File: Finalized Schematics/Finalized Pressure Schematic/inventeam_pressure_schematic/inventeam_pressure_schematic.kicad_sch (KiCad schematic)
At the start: 5 parts, among them J1 Conn_02x20_Top_Bottom

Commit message: Pressure V2.1
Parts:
- added TP1, TP10, TP11, TP12, TP13, TP14, TP15, TP16, TP17, TP18, TP19, TP2, TP20, TP21, TP22, TP23, TP24, TP25, TP26, TP27, TP28, TP29, TP3, TP30, TP31, TP32, TP33, TP34, TP35, TP36, TP37, TP38, TP4, TP5, TP6, TP7, TP8, TP9: TestPoint_Probe, TestPoint:TestPoint_Pad_D2.5mm, symbol Connector:TestPoint_Probe
- H1, H2, H3, H4: footprint (none) -> MountingHole:MountingHole_2.7mm_M2.5
- J1: footprint (none) -> Connector_PinHeader_2.54mm:PinHeader_2x20_P2.54mm_Vertical
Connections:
- net COL_1: now also TP1.1
- net COL_10: now also TP10.1
- net COL_11: now also TP11.1
- net COL_12: now also TP12.1
- net COL_13: now also TP13.1
- net COL_14: now also TP14.1
- net COL_15: now also TP15.1
- net COL_16: now also TP16.1
- net COL_17: now also TP17.1
- net COL_18: now also TP18.1
- net COL_19: now also TP19.1
- net COL_2: now also TP2.1
- net COL_20: now also TP20.1
- net COL_21: now also TP21.1
- net COL_22: now also TP22.1
- net COL_23: now also TP23.1
- net COL_24: now also TP24.1
- net COL_25: now also TP25.1
- net COL_26: now also TP26.1
- net COL_3: now also TP3.1
- net COL_4: now also TP4.1
- net COL_5: now also TP5.1
- net COL_6: now also TP6.1
- net COL_7: now also TP7.1
- net COL_8: now also TP8.1
- net COL_9: now also TP9.1
- net ROW_1: now also TP27.1
- net ROW_10: now also TP36.1
- net ROW_11: now also TP37.1
- net ROW_12: now also TP38.1
- net ROW_2: now also TP28.1
- net ROW_3: now also TP29.1
- net ROW_4: now also TP30.1
- net ROW_5: now also TP31.1
- net ROW_6: now also TP32.1
- net ROW_7: now also TP33.1
- net ROW_8: now also TP34.1
- net ROW_9: now also TP35.1
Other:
- sheet Row Matrix renamed Pressure Matrix
- removed sheet Column Matrix
- sheet Pressure Matrix: file row_matrix.kicad_sch -> pressure_matrix.kicad_sch
- sheet Pressure Matrix ports: added COL_1, COL_10, COL_11, COL_12, COL_13, COL_14, COL_15, COL_16, COL_17, COL_18, COL_19, COL_2, COL_20, COL_21, COL_22, COL_23, COL_24, COL_25, COL_26, COL_3, COL_4, COL_5, COL_6, COL_7, COL_8, COL_9; removed none
- note added: "Pressure Matrix"
- note added: "Test Points"
- note removed: "Column Matrix (hierarchical)"
- note removed: "Row Matrix (hierarchical)"
- moved on the sheet: H1, H2, H3, H4

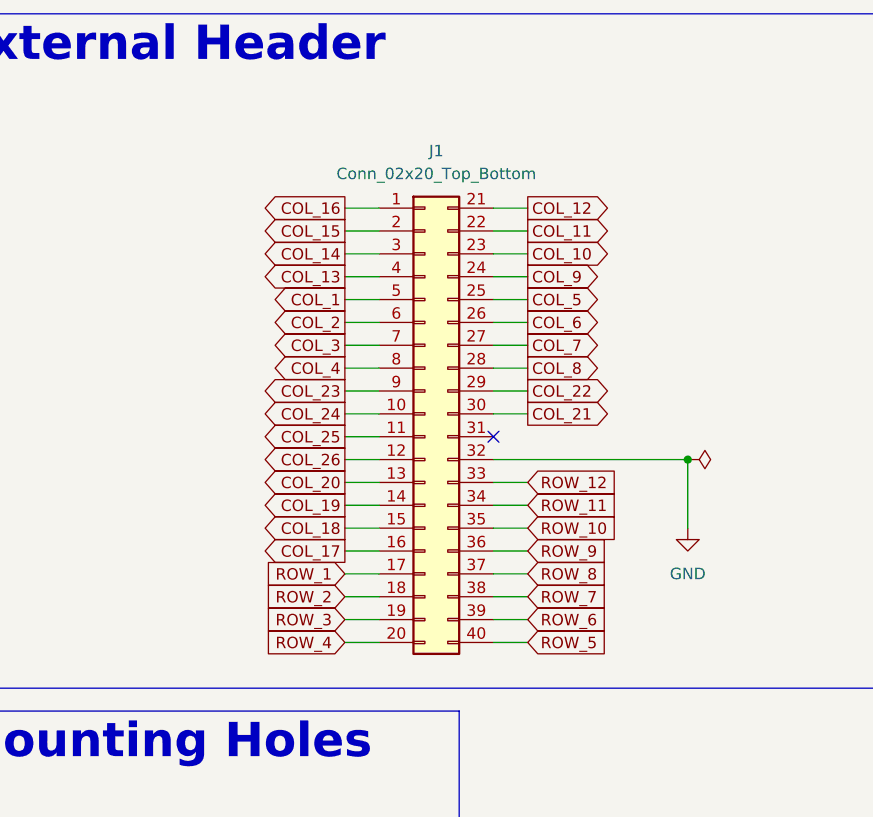
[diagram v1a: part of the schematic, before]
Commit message: Fixed header
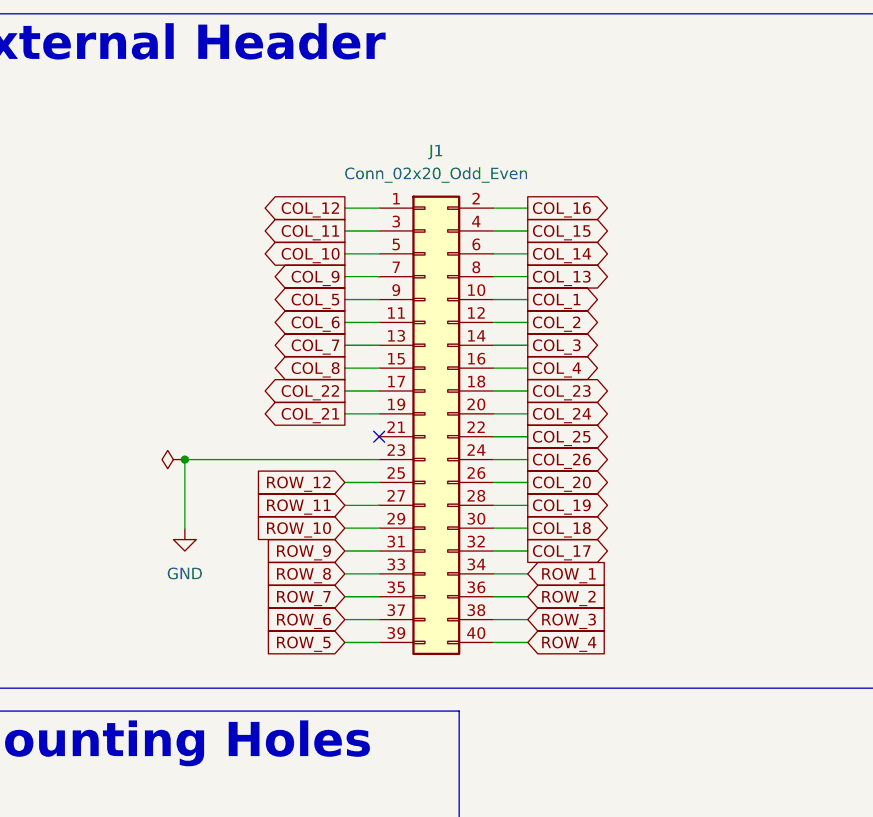
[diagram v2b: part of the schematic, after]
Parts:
- removed J1: Conn_02x20_Top_Bottom, Connector_PinHeader_2.54mm:PinHeader_2x20_P2.54mm_Vertical, symbol Connector_Generic:Conn_02x20_Top_Bottom
- added J1: Conn_02x20_Odd_Even, Connector_PinHeader_2.54mm:PinHeader_2x20_P2.54mm_Vertical, symbol Connector_Generic:Conn_02x20_Odd_Even
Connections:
- net COL_1: now also J1.10 (Pin_10)
- net COL_10: now also J1.5 (Pin_5)
- net COL_11: now also J1.3 (Pin_3)
- net COL_12: now also J1.1 (Pin_1)
- net COL_13: now also J1.8 (Pin_8)
- net COL_14: now also J1.6 (Pin_6)
- net COL_15: now also J1.4 (Pin_4)
- net COL_16: now also J1.2 (Pin_2)
- net COL_17: now also J1.32 (Pin_32)
- net COL_18: now also J1.30 (Pin_30)
- net COL_19: now also J1.28 (Pin_28)
- net COL_2: now also J1.12 (Pin_12)
- net COL_20: now also J1.26 (Pin_26)
- net COL_21: now also J1.19 (Pin_19)
- net COL_22: now also J1.17 (Pin_17)
- net COL_23: now also J1.18 (Pin_18)
- net COL_24: now also J1.20 (Pin_20)
- net COL_25: now also J1.22 (Pin_22)
- net COL_26: now also J1.24 (Pin_24)
- net COL_3: now also J1.14 (Pin_14)
- net COL_4: now also J1.16 (Pin_16)
- net COL_5: now also J1.9 (Pin_9)
- net COL_6: now also J1.11 (Pin_11)
- net COL_7: now also J1.13 (Pin_13)
- net COL_8: now also J1.15 (Pin_15)
- net COL_9: now also J1.7 (Pin_7)
- net GND: now also J1.23 (Pin_23)
- net ROW_1: now also J1.34 (Pin_34)
- net ROW_10: now also J1.29 (Pin_29)
- net ROW_11: now also J1.27 (Pin_27)
- net ROW_12: now also J1.25 (Pin_25)
- net ROW_2: now also J1.36 (Pin_36)
- net ROW_3: now also J1.38 (Pin_38)
- net ROW_4: now also J1.40 (Pin_40)
- net ROW_5: now also J1.39 (Pin_39)
- net ROW_6: now also J1.37 (Pin_37)
- net ROW_7: now also J1.35 (Pin_35)
- net ROW_8: now also J1.33 (Pin_33)
- net ROW_9: now also J1.31 (Pin_31)

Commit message: Pressure V2.2
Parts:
- added TP39: TestPoint_Probe, TestPoint:TestPoint_Pad_D2.5mm, symbol Connector:TestPoint_Probe
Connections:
- net GND: now also TP39.1
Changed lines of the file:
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@@
 		)
 	)
+	(wire
+		(pts
+			(xy 148.59 147.32) (xy 148.59 151.13)
+		)
+		(stroke
+			(width 0)
+			(type default)
+		)
+	)
 	(image
 		(at 260.35 111.76)
@@
 	(symbol
 		(lib_id "Connector:TestPoint_Probe")
+		(at 148.59 147.32 0)
+		(unit 1)
+		(exclude_from_sim no)
+		(in_bom yes)
+		(on_board yes)
+		(dnp no)
+		(property "Reference" "TP39"
+			(at 152.4 146.05 0)
+			(effects
+				(font
+					(size 1.27 1.27)
+				)
+				(justify left)
+			)
+		)
+		(property "Value" "TestPoint_Probe"
+			(at 152.4 147.0024 0)
+			(effects
+				(font
+					(size 1.27 1.27)
+				)
+				(justify left)
+				(hide yes)
+			)
+		)
+		(property "Footprint" "TestPoint:TestPoint_Pad_D2.5mm"
+			(at 153.67 147.32 0)
+			(effects
+				(font
+					(size 1.27 1.27)
+				)
+				(hide yes)
+			)
+		)
+		(property "Datasheet" "~"
+			(at 153.67 147.32 0)
+			(effects
+				(font
+					(size 1.27 1.27)
+				)
+				(hide yes)
+			)
+		)
+		(property "Description" "test point (alternative probe-style design)"
+			(at 148.59 147.32 0)
+			(effects
+				(font
+					(size 1.27 1.27)
+				)
+				(hide yes)
+			)
+		)
+		(pin "1"
+		)
+		(instances
+			(project "inventeam_pressure_schematic"
+				(path "/fcaa09fa-e29c-4184-8671-cd833b0ef719"
+					(reference "TP39")
+					(unit 1)
+				)
+			)
+		)
+	)
+	(symbol
+		(lib_id "Connector:TestPoint_Probe")
 		(at 137.16 147.32 0)
 		(unit 1)
@@
 					(unit 1)
 				)
+			)
+		)
+	)
+	(symbol
+		(lib_id "power:GND")
+		(at 148.59 151.13 0)
+		(mirror y)
+		(unit 1)
+		(exclude_from_sim no)
+		(in_bom yes)
+		(on_board yes)
+		(dnp no)
+		(fields_autoplaced yes)
+		(property "Reference" "#PWR02"
+			(at 148.59 157.48 0)
+			(effects
+				(font
+					(size 1.27 1.27)
+				)
+				(hide yes)
+			)
+		)
+		(property "Value" "GND"
+			(at 148.59 156.21 0)
+			(effects
+				(font
+					(size 1.27 1.27)
+				)
+			)
+		)
+		(property "Footprint" ""
+			(at 148.59 151.13 0)
+			(effects
+				(font
+					(size 1.27 1.27)
+				)
+				(hide yes)
+			)
+		)
+		(property "Datasheet" ""
+			(at 148.59 151.13 0)
+			(effects
+				(font
+					(size 1.27 1.27)
+				)
+				(hide yes)
+			)
+		)
+		(property "Description" "Power symbol creates a global label with name \"GND\" , ground"
+			(at 148.59 151.13 0)
+			(effects
+				(font
+					(size 1.27 1.27)
+				)
+				(hide yes)
+			)
+		)
+		(pin "1"
+		)
+		(instances
+			(project "inventeam_pressure_schematic"
+				(path "/fcaa09fa-e29c-4184-8671-cd833b0ef719"
+					(reference "#PWR02")
+					(unit 1)
+				)
